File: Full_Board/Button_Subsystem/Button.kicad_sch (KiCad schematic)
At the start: 3 parts

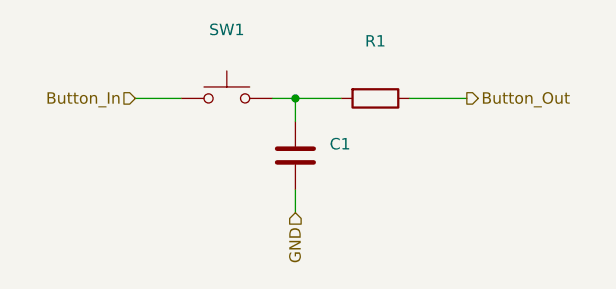
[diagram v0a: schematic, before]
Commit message: Worked on Power supply subsheet
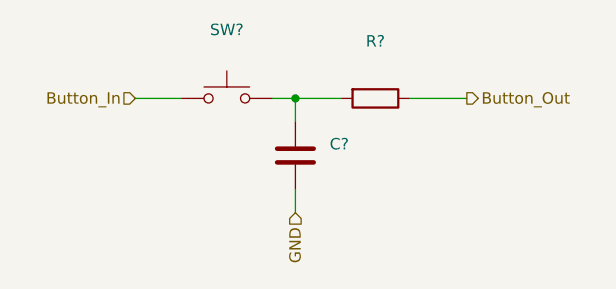
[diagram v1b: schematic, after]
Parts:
- renumbered C1 to C?, R1 to R?, SW1 to SW?
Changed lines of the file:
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@@
     (effects (font (size 1.27 1.27)) (justify left))
   )
-  (symbol (lib_id "Device:C") (at 118.11 101.6 0) (unit 1)
+  (symbol (lib_id "Device:C") (at 118.11 101.6 0)
     (in_bom yes) (on_board yes) (fields_autoplaced)
-    (property "Reference" "C1" (id 0) (at 121.92 100.3299 0)
+    (property "Reference" "C?" (id 0) (at 121.92 100.3299 0)
       (effects (font (size 1.27 1.27)) (justify left))
     )
@@
     (pin "2")
   )
-  (symbol (lib_id "Device:R") (at 127 95.25 270) (unit 1)
+  (symbol (lib_id "Device:R") (at 127 95.25 270)
     (in_bom yes) (on_board yes) (fields_autoplaced)
-    (property "Reference" "R1" (id 0) (at 127 88.9 90))
+    (property "Reference" "R?" (id 0) (at 127 88.9 90))
     (property "Value" "~" (id 1) (at 127 91.44 90))
     (property "Footprint" "" (id 2) (at 127 93.472 90)
@@
     (pin "2")
   )
-  (symbol (lib_id "Switch:SW_Push") (at 110.49 95.25 0) (unit 1)
+  (symbol (lib_id "Switch:SW_Push") (at 110.49 95.25 0)
     (in_bom yes) (on_board yes) (fields_autoplaced)
-    (property "Reference" "SW1" (id 0) (at 110.49 87.63 0))
+    (property "Reference" "SW?" (id 0) (at 110.49 87.63 0))
     (property "Value" "~" (id 1) (at 110.49 90.17 0))
     (property "Footprint" "" (id 2) (at 110.49 90.17 0)

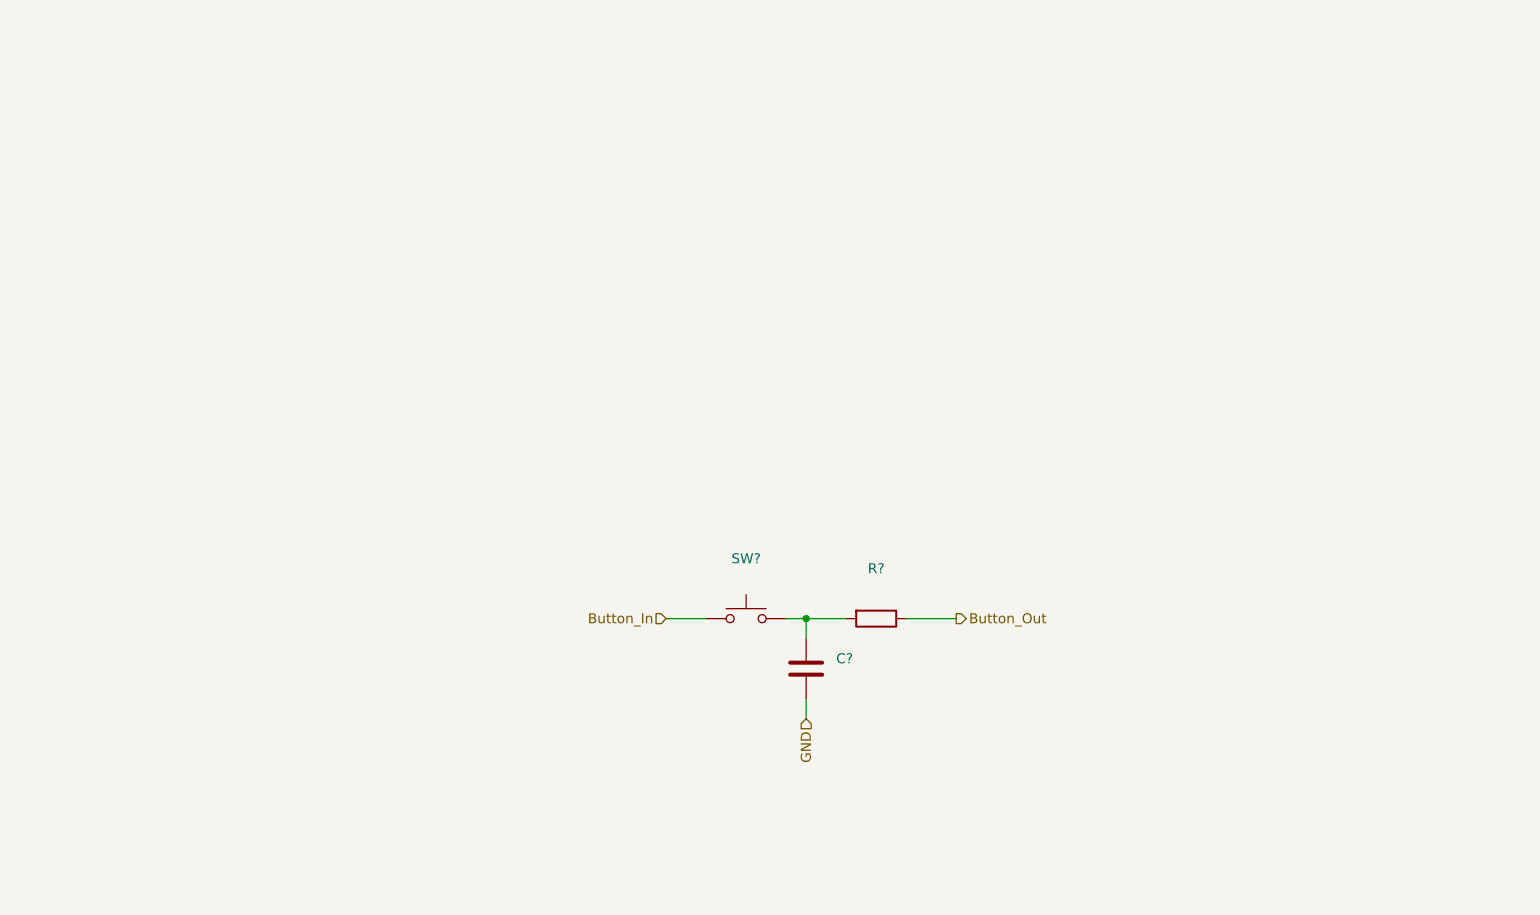
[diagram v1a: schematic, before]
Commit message: Finalize MSP432, stepper, and button subsheets
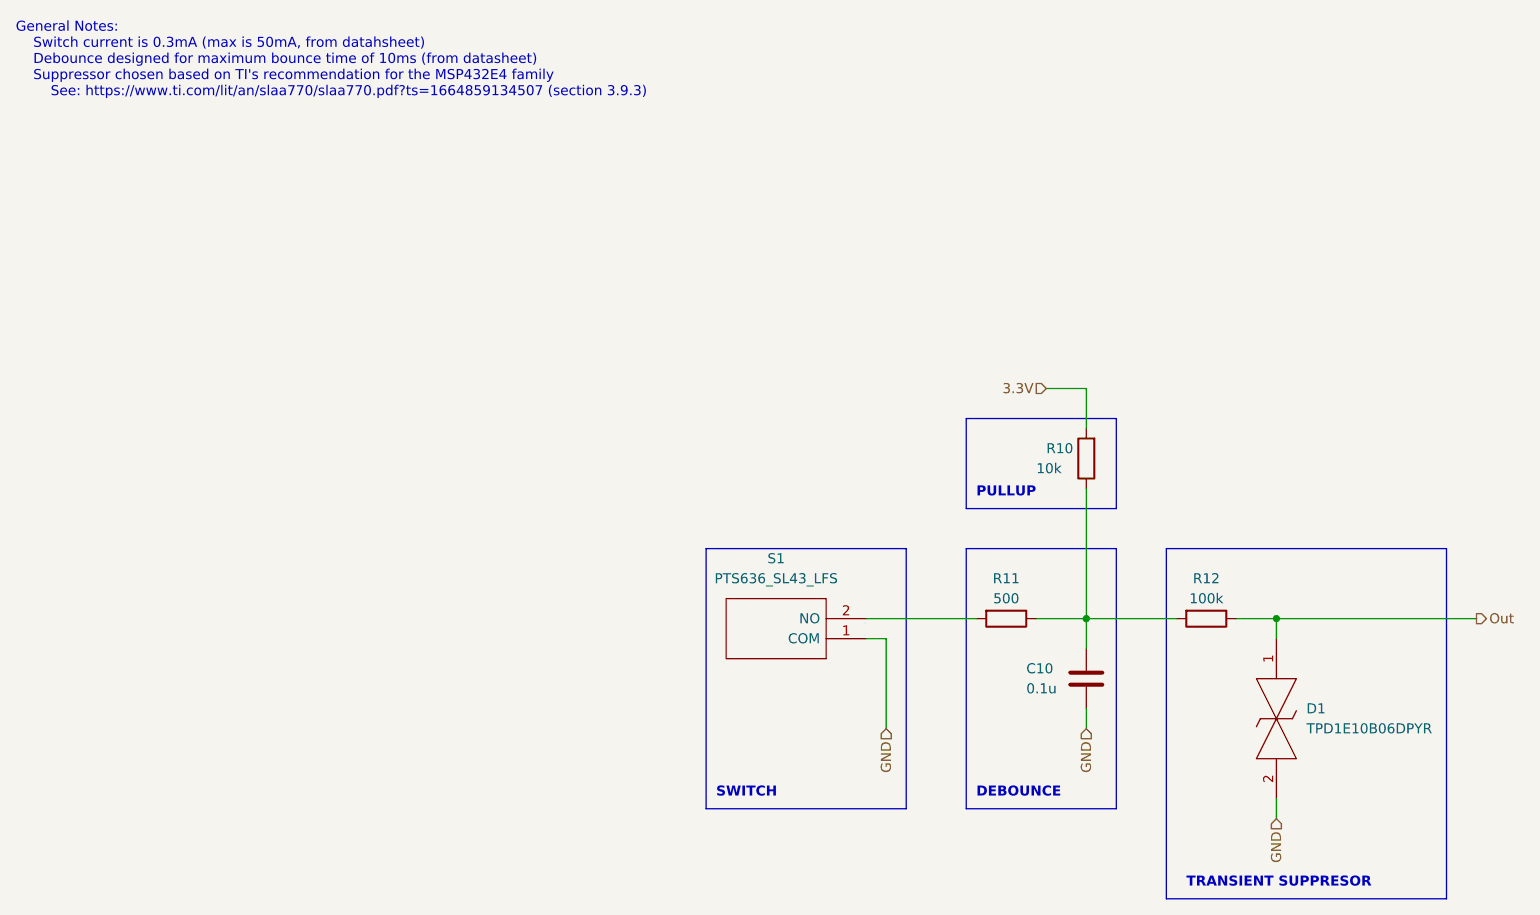
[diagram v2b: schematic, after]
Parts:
- removed C?: ~, symbol Device:C
- removed R?: ~, symbol Device:R
- removed SW?: ~, symbol Switch:SW_Push
- added C10: 0.1u, symbol Device:C
- added D1: TPD1E10B06DPYR, TPD1E10B06DPYR, symbol TPD1E10B06DPYR:TPD1E10B06DPYR
- added R10: 10k, symbol Device:R
- added R11: 500, symbol Device:R
- added R12: 100k, symbol Device:R
- added S1: PTS636_SL43_LFS, PTS636SL43LFS, symbol PTS636_SL43_LFS:PTS636_SL43_LFS
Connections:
- net GND: now also C10.2, D1.2, S1.1 (COM)
- new net: R11.2, S1.2 (NO)
- new net: C10.1, R10.1, R11.1, R12.2
- new net 3.3V: R10.2
- new net Out: D1.1, R12.1
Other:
- note added: "DEBOUNCE"
- note added: "General Notes: Switch current is 0.3mA (max is 50mA, from datahsheet) Debounce designed for maximum bounce time of 10ms (from datasheet) Suppressor chosen based on TI's recommendation for the MSP432E4 family See: https://www.ti.com/lit/an/slaa770/slaa770.pdf?ts=1664859134507 (section 3.9.3)"
- note added: "PULLUP"
- note added: "SWITCH"
- note added: "TRANSIENT SUPPRESOR"

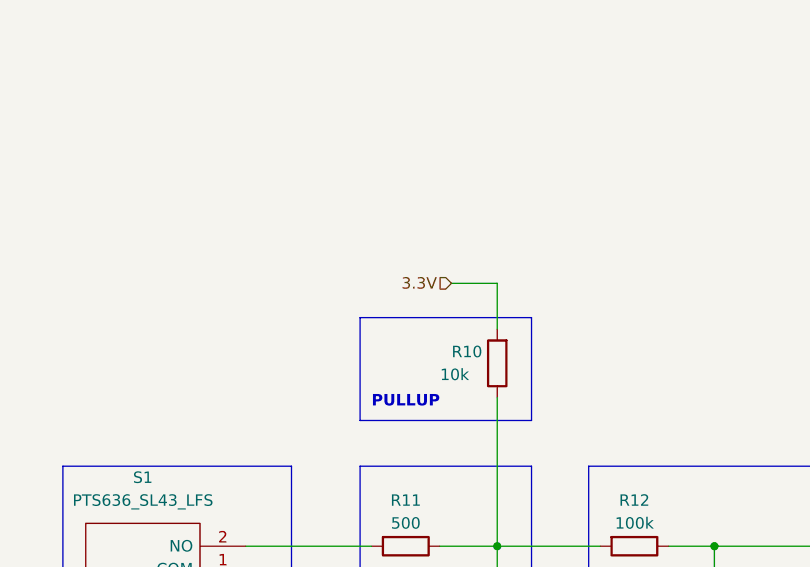
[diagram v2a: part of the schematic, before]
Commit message: Layout LED subsystem
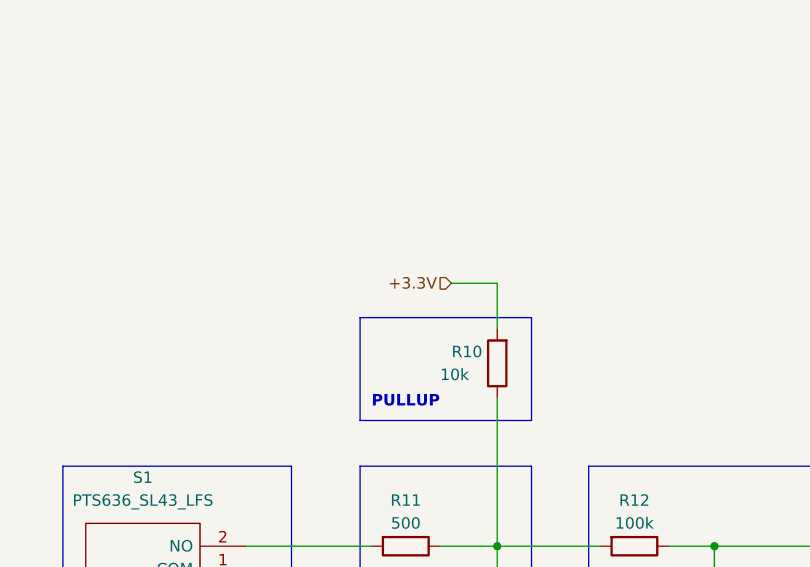
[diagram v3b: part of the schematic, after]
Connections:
- net 3.3V renamed +3.3V
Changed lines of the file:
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@@
     (effects (font (size 1.27 1.27)) (justify left))
   )
-  (hierarchical_label "3.3V" (shape input) (at 148.59 66.04 180)
+  (hierarchical_label "+3.3V" (shape input) (at 148.59 66.04 180)
     (effects (font (size 1.27 1.27)) (justify right))
   )

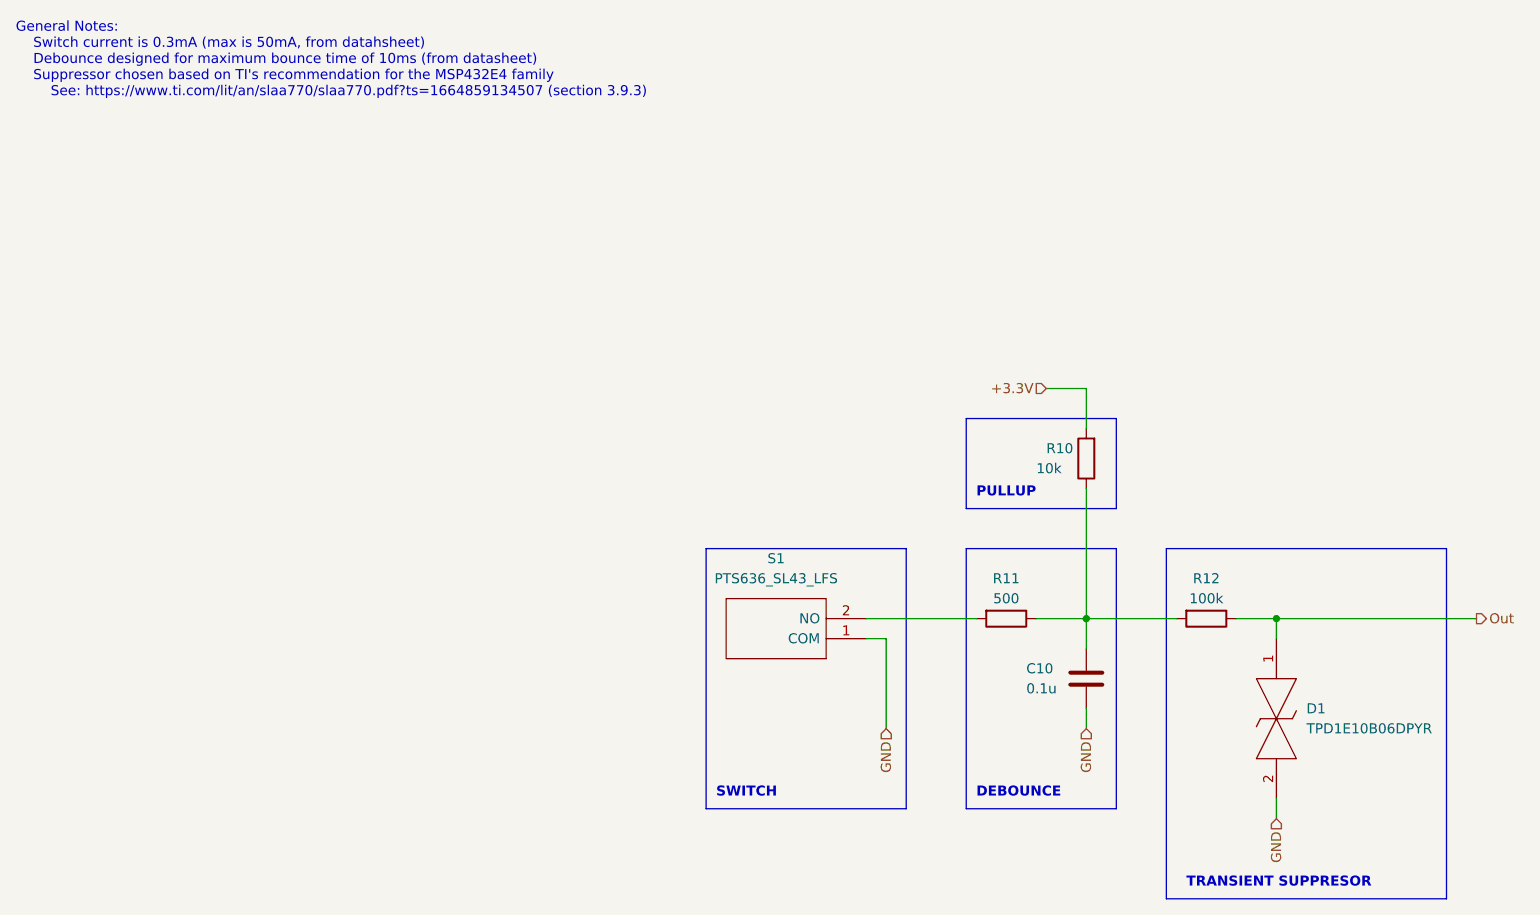
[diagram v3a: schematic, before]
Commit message: Add digikey/mouser components to stepper and button subsystems
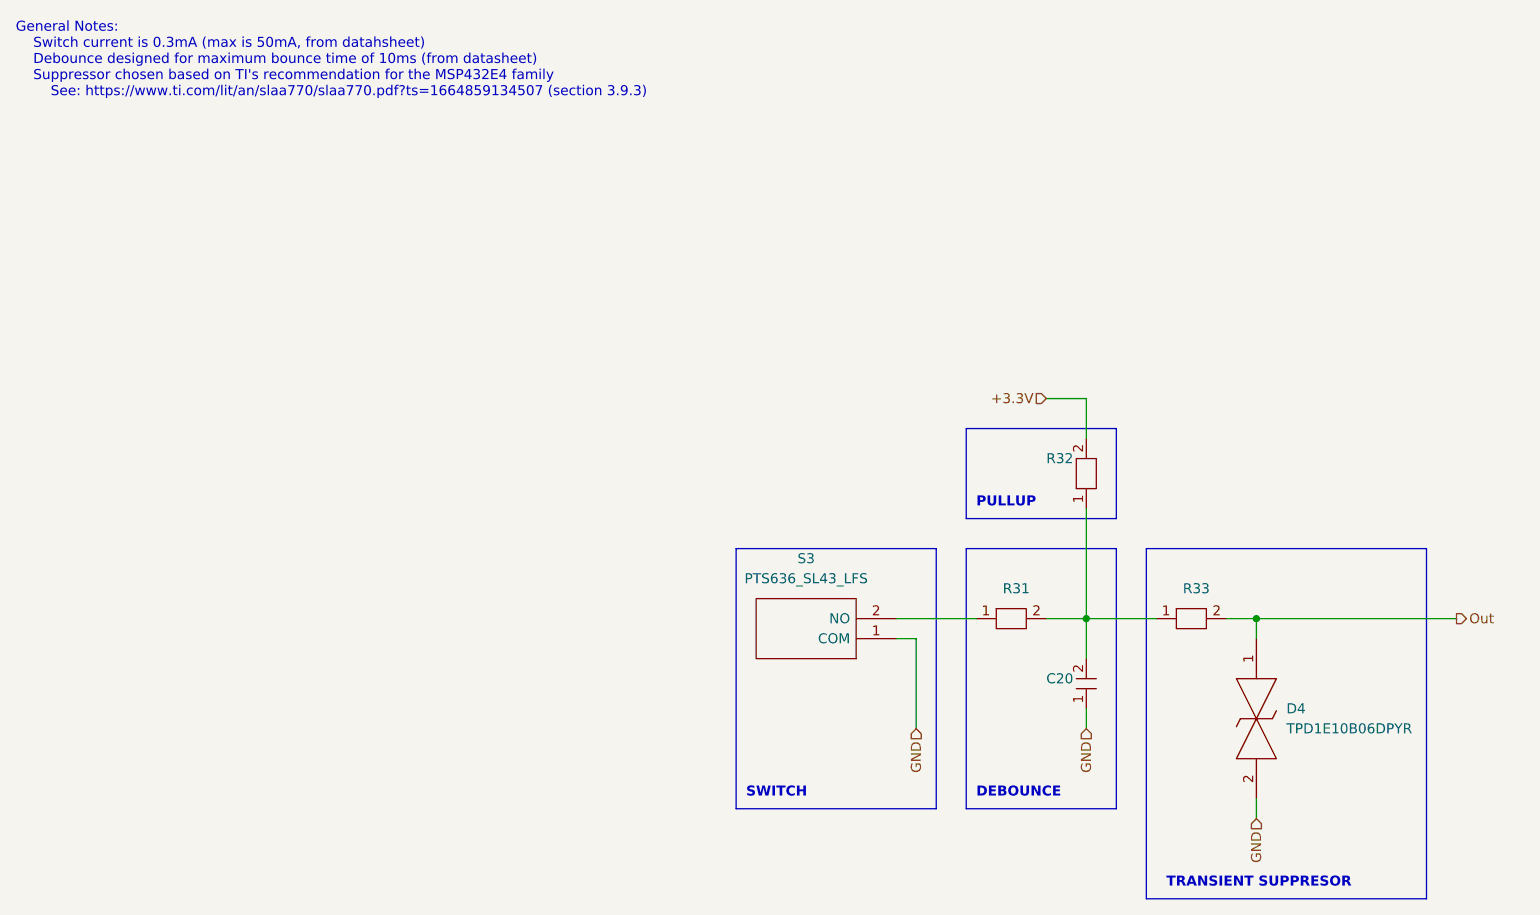
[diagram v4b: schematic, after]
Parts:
- removed C10: 0.1u, symbol Device:C
- removed R10: 10k, symbol Device:R
- removed R11: 500, symbol Device:R
- removed R12: 100k, symbol Device:R
- added C20: C1210C822K2RACAUTO, CAPC3225X88N, symbol C1210C822K2RACAUTO:C1210C822K2RACAUTO
- added R31: CR0402-FX-5620GLF, RESC1005X40N, symbol CR0402-FX-5620GLF:CR0402-FX-5620GLF
- added R32: CRMA1210AF10K0DKEF, RESC3225X74N, symbol CRMA1210AF10K0DKEF:CRMA1210AF10K0DKEF
- added R33: RCV2512100KFKEGAT, RESC6332X70N, symbol RCV2512100KFKEGAT:RCV2512100KFKEGAT
- renumbered D1 to D4, S1 to S3
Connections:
- net +3.3V: now also R32.2
- net GND: now also C20.1
- net Out: now also R33.2
- net at S3.2 (NO): now also R31.1
- new net: C20.2, R31.2, R32.1, R33.1
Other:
- moved on the sheet: D4, S3

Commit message: Add files via upload
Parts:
- C20: footprint CAPC3225X88N -> (none)
- D4: footprint TPD1E10B06DPYR -> Diode_Protection_TPD1:TPD1E10B06DPYR
- R31: footprint RESC1005X40N -> Resistor_Chip_CR0402-FX-5620GLF:RESC1005X40N
- R32: footprint RESC3225X74N -> Resistor_SMD:R_0201_0603Metric
- R33: footprint RESC6332X70N -> (none)
- S3: footprint PTS636SL43LFS -> (none)
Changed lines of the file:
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@@
     (property "Reference" "S3" (id 0) (at 118.11 87.63 0))
     (property "Value" "PTS636_SL43_LFS" (id 1) (at 118.11 90.17 0))
-    (property "Footprint" "PTS636SL43LFS" (id 2) (at 110.49 100.33 0)
+    (property "Footprint" "" (id 2) (at 110.49 100.33 0)
       (effects (font (size 1.27 1.27)) (justify left) hide)
     )
@@
       (effects (font (size 1.27 1.27)) (justify left))
     )
-    (property "Footprint" "TPD1E10B06DPYR" (id 2) (at 179.07 110.49 0)
+    (property "Footprint" "Diode_Protection_TPD1:TPD1E10B06DPYR" (id 2) (at 179.07 110.49 0)
       (effects (font (size 1.27 1.27)) (justify left bottom) hide)
     )
@@
       (effects (font (size 1.27 1.27)) (justify right) hide)
     )
-    (property "Footprint" "CAPC3225X88N" (id 2) (at 152.4 97.79 0)
+    (property "Footprint" "" (id 2) (at 152.4 97.79 0)
       (effects (font (size 1.27 1.27)) (justify left) hide)
     )
@@
       (effects (font (size 1.27 1.27)) (justify right) hide)
     )
-    (property "Footprint" "RESC3225X74N" (id 2) (at 152.4 67.31 0)
+    (property "Footprint" "Resistor_SMD:R_0201_0603Metric" (id 2) (at 152.4 67.31 0)
       (effects (font (size 1.27 1.27)) (justify left) hide)
     )
@@
       (effects (font (size 1.27 1.27)) hide)
     )
-    (property "Footprint" "RESC6332X70N" (id 2) (at 176.53 93.98 0)
+    (property "Footprint" "" (id 2) (at 176.53 93.98 0)
       (effects (font (size 1.27 1.27)) (justify left) hide)
     )
@@
       (effects (font (size 1.27 1.27)) hide)
     )
-    (property "Footprint" "RESC1005X40N" (id 2) (at 153.67 93.98 0)
+    (property "Footprint" "Resistor_Chip_CR0402-FX-5620GLF:RESC1005X40N" (id 2) (at 153.67 93.98 0)
       (effects (font (size 1.27 1.27)) (justify left) hide)
     )

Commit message: Added footprint for the switches
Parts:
- S3: footprint (none) -> PTS636_SL43_LFS:PTS636SL43LFS
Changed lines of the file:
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@@
     (property "Reference" "S3" (id 0) (at 118.11 87.63 0))
     (property "Value" "PTS636_SL43_LFS" (id 1) (at 118.11 90.17 0))
-    (property "Footprint" "" (id 2) (at 110.49 100.33 0)
+    (property "Footprint" "PTS636_SL43_LFS:PTS636SL43LFS" (id 2) (at 110.49 100.33 0)
       (effects (font (size 1.27 1.27)) (justify left) hide)
     )
